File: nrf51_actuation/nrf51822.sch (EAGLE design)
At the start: 22 parts, among them T1 MMUN2238

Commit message: Sensor board should be 100% done... Waiting for boards from slow china :0)
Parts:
- removed CR2450: 3.3V, NordicSemi:CR2450
- removed PIR: EKMB1303112, NordicSemi:EKMB1303112
- removed SI7021: SI7021SMD, NordicSemi:SI7021SMD
- removed SW1: (no value), microbuilder:SWITCH_PUSHBUTTONSOFTTOUCHSMD_SJ
- removed TMP36: TMP36_SOT23_5, NordicSemi:TMP36_SOT23_5
- removed TSL2561: LIGHT_TSL2561, microbuilder:LIGHT_TSL2561
- removed U$6, U$7: MOUNTINGHOLE2.5, microbuilder:MOUNTINGHOLE2.5
- added ACS712_20A: ACS712, SparkFun-AnalogIC:ACS712
- added ADP121: (no value), microbuilder:ADP121
- added C4, C5: 10uF, rcl:C-EUC0805
- added FTR-K3AB: FTR-K3AB, NordicSemi:FTR-K3AB
- added J1, J2, J3, J4: (no value), microbuilder:TERMBLOCK_1X2
- added R1, R2: (no value), microbuilder:RESISTOR0805
- C1: value 100nF -> 1nF
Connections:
- removed net GIOP3: SW1.P$2, U$4.P0.11
- new net 5.0V: ACS712_20A.VCC, ADP121.EN, ADP121.IN, C2.1, C5.1, FTR-K3ABG$2.1, J3.1
- new net N$11: ACS712_20A.FILT, C1.1
- new net N$15: ACS712_20A.VOUT, R1.1
- new net ROUT1: ACS712_20A.IP+@1, ACS712_20A.IP+@2, FTR-K3ABG$1.4, J2.1, J4.1
- new net ROUT2: ACS712_20A.IP-@3, ACS712_20A.IP-@4, FTR-K3ABG$1.3, J2.2, J4.2
- new net TERMO1: J1.1
- new net TERMO2: J1.2
- net AIN0/XL2: now also R1.2, R2.1
- net AIN2: no longer TMP36.+VS, TMP36.SHTD
- net AIN3: no longer TMP36.VOUT
- net AIN5: no longer PIR.OUT
- net AIN6: no longer PIR.VDD
- net GIOP0: no longer TSL2561.SDA
- net GIOP1: no longer TSL2561.SCL
- net GIOP5: no longer SI7021.SDA
- net GIOP6: no longer SI7021.SCL
- net GIOP7: no longer C2.1, SI7021.VDD
- net GND: now also ACS712_20A.GND, ADP121.GND, C1.2, C4.2, C5.2, J3.2, R2.2; no longer PIR.GND, SI7021.GND, SW1.P$1, TMP36.GND
- net N$7: now also FTR-K3ABG$2.2; no longer C1.1, TSL2561.GND
- net VDD: now also ADP121.OUT, C4.1; no longer C1.2, TSL2561.3.3V
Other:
- note removed: "BATT"
- note removed: "HIGH DRIVE"
- note removed: "HUMIDITY+TEMP"
- note removed: "LIGHT"
- note removed: "NC"
- note removed: "TEMP"
- note removed: "USE INTERNAL PULLUP"
- moved on the sheet: C1, C2, T1

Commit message: Done with routing.. should be more or less done
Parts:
- removed J3: (no value), microbuilder:TERMBLOCK_1X2
- added AD8495: AD8495, NordicSemi:AD8495
- added C12: 100nF, rcl:C-EUC0805
- added C13, C14: 12pF, rcl:C-EUC0805
- added C6: 10nF, rcl:C-EUC0805
- added FB1, FB2: (no value), microbuilder:FERRITE0805
- added IRM-05-5: IRM05-5V, NordicSemi:IRM05-5V
- added U$1, U$13, U$14, U$7: MOUNTINGHOLE2.5, microbuilder:MOUNTINGHOLE2.5
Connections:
- removed net ROUT1: ACS712_20A.IP+@1, ACS712_20A.IP+@2, FTR-K3ABG$1.4, J2.1, J4.1
- removed net ROUT2: ACS712_20A.IP-@3, ACS712_20A.IP-@4, FTR-K3ABG$1.3, J2.2, J4.2
- removed net TERMO1: J1.1
- removed net TERMO2: J1.2
- new net AC/L: ACS712_20A.IP+@1, ACS712_20A.IP+@2, IRM-05-5.AC/L, J4.1
- new net AC/LOUT: ACS712_20A.IP-@3, ACS712_20A.IP-@4, J2.2
- new net AC/N: FTR-K3ABG$1.3, IRM-05-5.AC/N, J4.2
- new net AC/NOUT: FTR-K3ABG$1.4, J2.1
- new net GIOP10: U$4.P0.17
- new net GIOP3: U$4.P0.11
- new net N$16: AD8495.-IN, C6.2, FB2.P$2
- new net N$17: FB2.P$1, J1.2
- new net N$8: FB1.P$1, J1.1
- new net N$9: AD8495.+IN, C6.1, FB1.P$2
- net 5.0V: now also AD8495.+VS, C12.2, IRM-05-5.+V; no longer J3.1
- net AIN4: now also AD8495.OUT, AD8495.SENSE
- net GND: now also AD8495.GND, AD8495.REF, C12.1, C13.1, C14.1, IRM-05-5.-V; no longer J3.2
- net N$1: now also C14.2, CRST1.H2, U$4.XC2; no longer CRST1.H1, U$4.XC1
- net N$2: now also C13.2, CRST1.H1, U$4.XC1; no longer CRST1.H2, U$4.XC2
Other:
- note added: "THERMO"
- moved on the sheet: ANT, BALUN, C10, C11, C3, C7, C8, C9, CRST1, J1, J2, J4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

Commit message: CLEANED AND ADDED COMMENTS / TAGS ACTUATION MADE 45% SMALLER
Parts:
- removed U$13, U$14: MOUNTINGHOLE2.5, microbuilder:MOUNTINGHOLE2.5
- R1: value (none) -> 2k
- R2: value (none) -> 8k
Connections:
- net AC/L: now also FTR-K3ABG$1.4; no longer ACS712_20A.IP+@1, ACS712_20A.IP+@2
- net AC/LOUT: now also FTR-K3ABG$1.3, J2.1; no longer ACS712_20A.IP-@3, ACS712_20A.IP-@4, J2.2
- net AC/N: now also ACS712_20A.IP+@1, ACS712_20A.IP+@2; no longer FTR-K3ABG$1.3
- net AC/NOUT: now also ACS712_20A.IP-@3, ACS712_20A.IP-@4, J2.2; no longer FTR-K3ABG$1.4, J2.1
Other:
- note added: "AC IN"
- note added: "AC OUT"
- note added: "AC/DC"
- note added: "DC/DC"
- note added: "HALL EFFECT"
- note added: "MOUNT HOLES"
- note added: "PROG HEADER"
- note added: "RELAY"
- note added: "THERMOCOUPLE COLD JUNCTION"
- note removed: "THERMO"
- moved on the sheet: AD8495, C12, C6, FB1, FB2, J1, J2

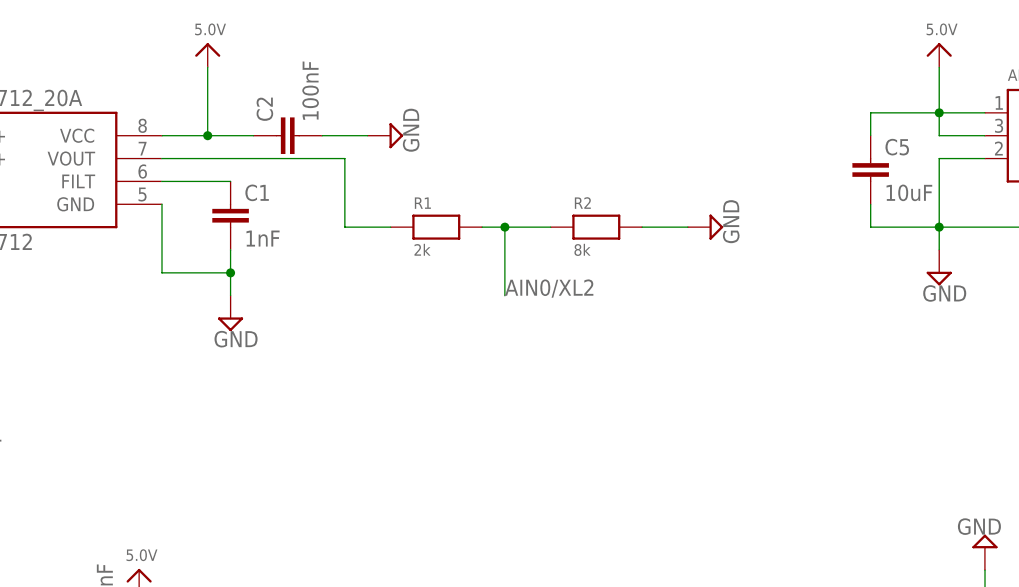
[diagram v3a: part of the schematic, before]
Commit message: Added optional low pass filter circut and cleaned up some more
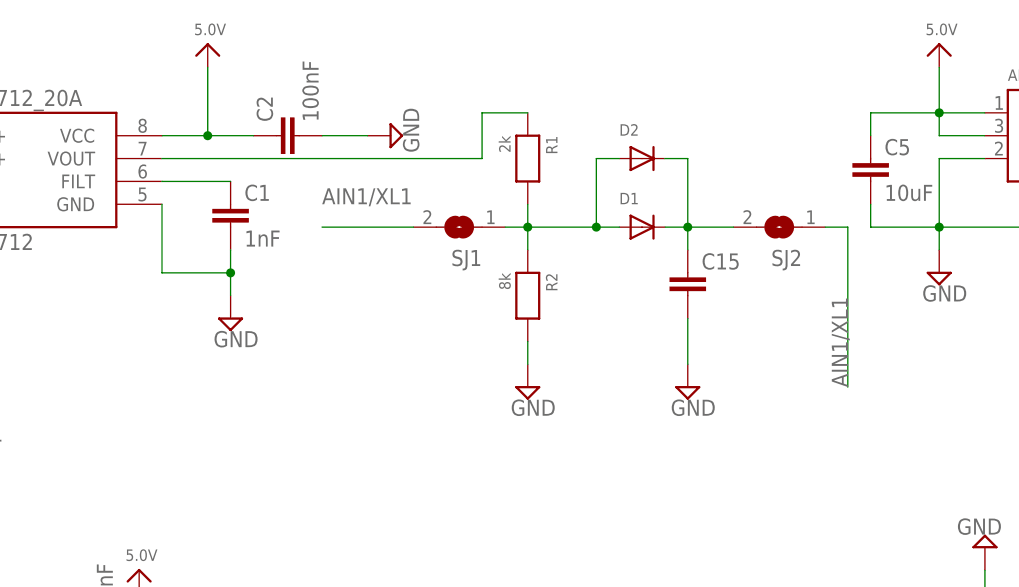
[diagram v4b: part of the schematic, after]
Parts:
- added C15: (no value), SparkFun-Capacitors:CAPPTH3
- added D1: (no value), adafruit:DIODESOD-123
- added D2: (no value), microbuilder:DIODEDO-1N4148
- added SJ1, SJ2: SOLDERJUMPERREFLOW_NOPASTE, microbuilder:SOLDERJUMPERREFLOW_NOPASTE
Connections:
- new net N$15: D1.A, D2.A, R1.2, R2.1, SJ1.1
- new net N$19: C15.1, D1.C, D2.C, SJ2.2
- net AIN0/XL2: no longer R1.2, R2.1
- net AIN1/XL1: now also SJ1.2, SJ2.1
- net GND: now also C15.2
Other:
- moved on the sheet: R1, R2
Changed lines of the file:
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@@
 <part name="U$1" library="microbuilder" deviceset="MOUNTINGHOLE" device="2.5"/>
 <part name="U$7" library="microbuilder" deviceset="MOUNTINGHOLE" device="2.5"/>
+<part name="SJ2" library="microbuilder" deviceset="SOLDERJUMPER" device="REFLOW_NOPASTE"/>
+<part name="D1" library="adafruit" deviceset="DIODE" device="SOD-123"/>
+<part name="C15" library="SparkFun-Capacitors" deviceset="CAP" device="PTH3"/>
+<part name="D2" library="microbuilder" deviceset="DIODE" device="DO-1N4148"/>
+<part name="SUPPLY14" library="supply2" deviceset="GND" device=""/>
+<part name="SJ1" library="microbuilder" deviceset="SOLDERJUMPER" device="REFLOW_NOPASTE"/>
 </parts>
 <sheets>
@@
 <instance part="FRAME1" gate="G$1" x="-88.9" y="-20.32"/>
 <instance part="ACS712_20A" gate="G$1" x="-43.18" y="139.7"/>
-<instance part="R1" gate="G$1" x="0" y="134.62"/>
-<instance part="R2" gate="G$1" x="17.78" y="134.62"/>
+<instance part="R1" gate="G$1" x="10.16" y="142.24" rot="R270"/>
+<instance part="R2" gate="G$1" x="10.16" y="127" rot="R270"/>
 <instance part="SUPPLY13" gate="GND" x="-22.86" y="124.46"/>
 <instance part="C1" gate="G$1" x="-22.86" y="137.16"/>
@@
 <instance part="SUPPLY15" gate="GND" x="-5.08" y="144.78" rot="R90"/>
 <instance part="U$8" gate="G$1" x="-25.4" y="154.94"/>
-<instance part="SUPPLY6" gate="GND" x="30.48" y="134.62" rot="R90"/>
+<instance part="SUPPLY6" gate="GND" x="10.16" y="116.84"/>
 <instance part="J4" gate="G$1" x="121.92" y="137.16" rot="MR0"/>
 <instance part="FTR-K3AB" gate="G$1" x="-48.26" y="15.24" rot="R270"/>
@@
 <instance part="U$1" gate="G$1" x="160.02" y="10.16"/>
 <instance part="U$7" gate="G$1" x="177.8" y="10.16"/>
+<instance part="SJ2" gate="1" x="38.1" y="134.62" smashed="yes" rot="R180">
+<attribute name="NAME" x="40.64" y="132.08" size="1.778" layer="95" rot="R180"/>
+</instance>
+<instance part="D1" gate="G$1" x="22.86" y="134.62"/>
+<instance part="C15" gate="G$1" x="27.94" y="127"/>
+<instance part="D2" gate="G$1" x="22.86" y="142.24"/>
+<instance part="SUPPLY14" gate="GND" x="27.94" y="116.84"/>
+<instance part="SJ1" gate="1" x="2.54" y="134.62" smashed="yes" rot="R180">
+<attribute name="NAME" x="5.08" y="132.08" size="1.778" layer="95" rot="R180"/>
+</instance>
 </instances>
 <busses>
@@
 <pinref part="R2" gate="G$1" pin="2"/>
 <pinref part="SUPPLY6" gate="GND" pin="GND"/>
-<wire x1="22.86" y1="134.62" x2="27.94" y2="134.62" width="0.1524" layer="91"/>
+<wire x1="10.16" y1="121.92" x2="10.16" y2="119.38" width="0.1524" layer="91"/>
 </segment>
 <segment>
@@
 <junction x="86.36" y="119.38"/>
 </segment>
+<segment>
+<pinref part="C15" gate="G$1" pin="2"/>
+<pinref part="SUPPLY14" gate="GND" pin="GND"/>
+<wire x1="27.94" y1="124.46" x2="27.94" y2="119.38" width="0.1524" layer="91"/>
+</segment>
 </net>
 <net name="VDD" class="0">
@@
 <net name="AIN0/XL2" class="0">
 <segment>
-<pinref part="R1" gate="G$1" pin="2"/>
-<pinref part="R2" gate="G$1" pin="1"/>
-<wire x1="5.08" y1="134.62" x2="7.62" y2="134.62" width="0.1524" layer="91"/>
-<wire x1="7.62" y1="134.62" x2="12.7" y2="134.62" width="0.1524" layer="91"/>
-<wire x1="7.62" y1="134.62" x2="7.62" y2="127" width="0.1524" layer="91"/>
-<junction x="7.62" y="134.62"/>
-<label x="7.62" y="127" size="1.778" layer="95"/>
-</segment>
-<segment>
 <pinref part="U$4" gate="G$1" pin="P0.26"/>
 <wire x1="58.42" y1="81.28" x2="58.42" y2="83.82" width="0.1524" layer="91"/>
@@
 </segment>
 </net>
-<net name="N$15" class="0">
-<segment>
-<pinref part="ACS712_20A" gate="G$1" pin="VOUT"/>
-<wire x1="-30.48" y1="142.24" x2="-10.16" y2="142.24" width="0.1524" layer="91"/>
-<wire x1="-10.16" y1="142.24" x2="-10.16" y2="134.62" width="0.1524" layer="91"/>
-<pinref part="R1" gate="G$1" pin="1"/>
-<wire x1="-10.16" y1="134.62" x2="-5.08" y2="134.62" width="0.1524" layer="91"/>
-</segment>
-</net>
 <net name="N$7" class="0">
 <segment>
@@
 <wire x1="55.88" y1="81.28" x2="55.88" y2="83.82" width="0.1524" layer="91"/>
 <label x="55.88" y="78.74" size="1.778" layer="95" rot="R90"/>
+</segment>
+<segment>
+<pinref part="SJ2" gate="1" pin="1"/>
+<wire x1="43.18" y1="134.62" x2="45.72" y2="134.62" width="0.1" layer="91"/>
+<wire x1="45.72" y1="134.62" x2="45.72" y2="116.84" width="0.1" layer="91"/>
+<label x="45.72" y="116.84" size="1.778" layer="95" rot="R90"/>
+</segment>
+<segment>
+<pinref part="SJ1" gate="1" pin="2"/>
+<wire x1="-2.54" y1="134.62" x2="-12.7" y2="134.62" width="0.1" layer="91"/>
+<label x="-12.7" y="137.16" size="1.778" layer="95"/>
 </segment>
 </net>
@@
 </segment>
 </net>
+<net name="N$18" class="0">
+<segment>
+<pinref part="ACS712_20A" gate="G$1" pin="VOUT"/>
+<wire x1="-30.48" y1="142.24" x2="5.08" y2="142.24" width="0.1524" layer="91"/>
+<wire x1="5.08" y1="142.24" x2="5.08" y2="147.32" width="0.1524" layer="91"/>
+<pinref part="R1" gate="G$1" pin="1"/>
+<wire x1="5.08" y1="147.32" x2="10.16" y2="147.32" width="0.1524" layer="91"/>
+</segment>
+</net>
+<net name="N$19" class="0">
+<segment>
+<pinref part="D2" gate="G$1" pin="C"/>
+<wire x1="25.4" y1="142.24" x2="27.94" y2="142.24" width="0.1524" layer="91"/>
+<pinref part="D1" gate="G$1" pin="C"/>
+<pinref part="SJ2" gate="1" pin="2"/>
+<wire x1="25.4" y1="134.62" x2="27.94" y2="134.62" width="0.1524" layer="91"/>
+<pinref part="C15" gate="G$1" pin="1"/>
+<wire x1="27.94" y1="134.62" x2="33.02" y2="134.62" width="0.1524" layer="91"/>
+<wire x1="27.94" y1="132.08" x2="27.94" y2="134.62" width="0.1524" layer="91"/>
+<junction x="27.94" y="134.62"/>
+<wire x1="27.94" y1="142.24" x2="27.94" y2="134.62" width="0.1524" layer="91"/>
+</segment>
+</net>
+<net name="N$15" class="0">
+<segment>
+<pinref part="R1" gate="G$1" pin="2"/>
+<pinref part="R2" gate="G$1" pin="1"/>
+<wire x1="10.16" y1="137.16" x2="10.16" y2="134.62" width="0.1" layer="91"/>
+<pinref part="SJ1" gate="1" pin="1"/>
+<pinref part="D1" gate="G$1" pin="A"/>
+<wire x1="10.16" y1="134.62" x2="10.16" y2="132.08" width="0.1" layer="91"/>
+<wire x1="7.62" y1="134.62" x2="10.16" y2="134.62" width="0.1" layer="91"/>
+<junction x="10.16" y="134.62"/>
+<wire x1="10.16" y1="134.62" x2="17.78" y2="134.62" width="0.1" layer="91"/>
+<pinref part="D2" gate="G$1" pin="A"/>
+<wire x1="17.78" y1="134.62" x2="20.32" y2="134.62" width="0.1" layer="91"/>
+<wire x1="20.32" y1="142.24" x2="17.78" y2="142.24" width="0.1" layer="91"/>
+<wire x1="17.78" y1="142.24" x2="17.78" y2="134.62" width="0.1" layer="91"/>
+<junction x="17.78" y="134.62"/>
+</segment>
+</net>

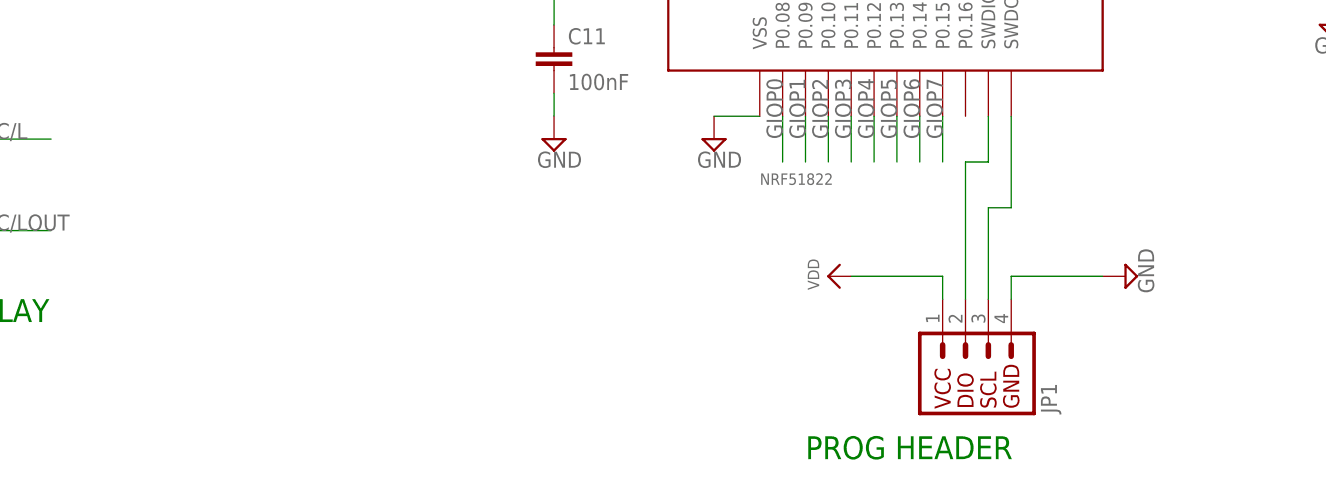
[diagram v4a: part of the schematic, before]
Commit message: Added a TMP36 sensor to ensure a power cutoff if the temperature rises above a threshold (in case of fire or shortcut)
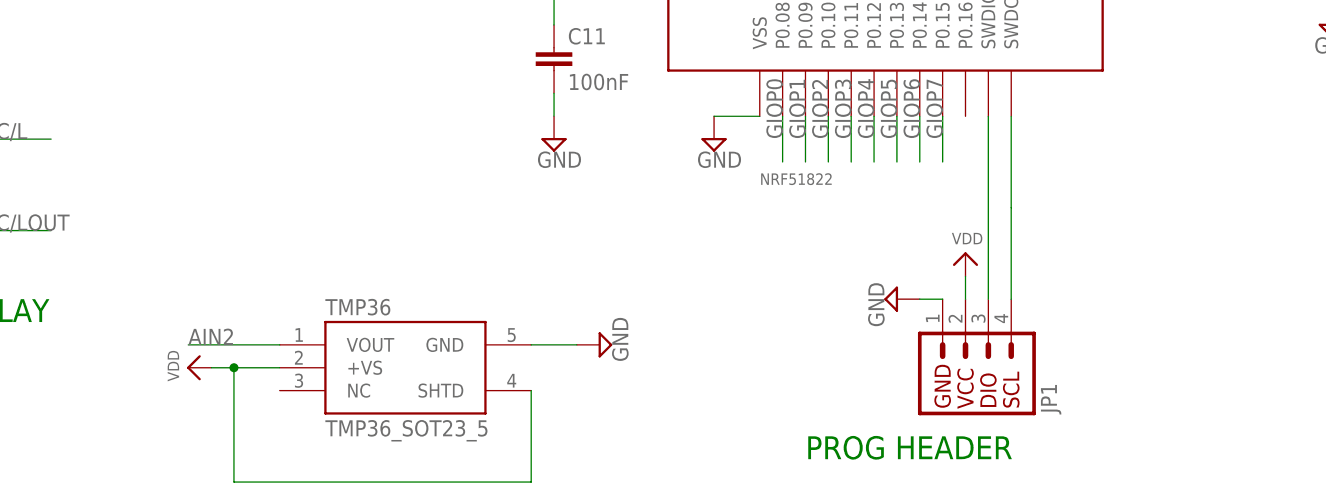
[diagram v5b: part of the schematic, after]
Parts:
- added TMP36: TMP36_SOT23_5, NordicSemi:TMP36_SOT23_5
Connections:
- net AIN2: now also TMP36.VOUT
- net GND: now also JP1.1, TMP36.GND; no longer JP1.4
- net N$12: now also JP1.3; no longer JP1.2
- net N$14: now also JP1.4; no longer JP1.3
- net VDD: now also JP1.2, TMP36.+VS, TMP36.SHTD; no longer JP1.1
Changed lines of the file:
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@@
 <part name="SUPPLY14" library="supply2" deviceset="GND" device=""/>
 <part name="SJ1" library="microbuilder" deviceset="SOLDERJUMPER" device="REFLOW_NOPASTE"/>
+<part name="TMP36" library="NordicSemi" deviceset="TMP36_SOT23_5" device=""/>
+<part name="SUPPLY20" library="supply2" deviceset="GND" device=""/>
+<part name="U$14" library="microbuilder" deviceset="VDD" device=""/>
 </parts>
 <sheets>
@@
 <instance part="BG" gate="G$1" x="119.38" y="99.06"/>
 <instance part="U$5" gate="G$1" x="27.94" y="43.18"/>
-<instance part="SUPPLY19" gate="GND" x="91.44" y="5.08" rot="R90"/>
-<instance part="U$3" gate="G$1" x="58.42" y="5.08" rot="R90"/>
+<instance part="SUPPLY19" gate="GND" x="66.04" y="2.54" rot="R270"/>
+<instance part="U$3" gate="G$1" x="73.66" y="7.62"/>
 <instance part="JP1" gate="G$1" x="68.58" y="-7.62" rot="MR90"/>
 <instance part="SUPPLY21" gate="GND" x="86.36" y="121.92" rot="R180"/>
@@
 <attribute name="NAME" x="5.08" y="132.08" size="1.778" layer="95" rot="R180"/>
 </instance>
+<instance part="TMP36" gate="G$1" x="10.16" y="-5.08"/>
+<instance part="SUPPLY20" gate="GND" x="33.02" y="-2.54" rot="R90"/>
+<instance part="U$14" gate="G$1" x="-12.7" y="-5.08" rot="R90"/>
 </instances>
 <busses>
@@
 </segment>
 <segment>
-<pinref part="SUPPLY19" gate="GND" pin="GND"/>
-<pinref part="JP1" gate="G$1" pin="4"/>
-<wire x1="88.9" y1="5.08" x2="78.74" y2="5.08" width="0.1524" layer="91"/>
-<wire x1="78.74" y1="5.08" x2="78.74" y2="2.54" width="0.1524" layer="91"/>
-</segment>
-<segment>
 <pinref part="C14" gate="G$1" pin="1"/>
 <pinref part="SUPPLY21" gate="GND" pin="GND"/>
@@
 <pinref part="SUPPLY14" gate="GND" pin="GND"/>
 <wire x1="27.94" y1="124.46" x2="27.94" y2="119.38" width="0.1524" layer="91"/>
+</segment>
+<segment>
+<pinref part="TMP36" gate="G$1" pin="GND"/>
+<pinref part="SUPPLY20" gate="GND" pin="GND"/>
+<wire x1="25.4" y1="-2.54" x2="30.48" y2="-2.54" width="0.1" layer="91"/>
+</segment>
+<segment>
+<pinref part="JP1" gate="G$1" pin="1"/>
+<pinref part="SUPPLY19" gate="GND" pin="GND"/>
+<wire x1="71.12" y1="2.54" x2="68.58" y2="2.54" width="0.1" layer="91"/>
 </segment>
 </net>
@@
 </segment>
 <segment>
+<pinref part="TMP36" gate="G$1" pin="+VS"/>
+<pinref part="U$14" gate="G$1" pin="VDD"/>
+<wire x1="-2.54" y1="-5.08" x2="-7.62" y2="-5.08" width="0.1" layer="91"/>
+<pinref part="TMP36" gate="G$1" pin="SHTD"/>
+<wire x1="-7.62" y1="-5.08" x2="-10.16" y2="-5.08" width="0.1" layer="91"/>
+<wire x1="25.4" y1="-7.62" x2="25.4" y2="-17.78" width="0.1" layer="91"/>
+<wire x1="25.4" y1="-17.78" x2="-7.62" y2="-17.78" width="0.1" layer="91"/>
+<wire x1="-7.62" y1="-17.78" x2="-7.62" y2="-5.08" width="0.1" layer="91"/>
+<junction x="-7.62" y="-5.08"/>
+</segment>
+<segment>
 <pinref part="U$3" gate="G$1" pin="VDD"/>
-<pinref part="JP1" gate="G$1" pin="1"/>
-<wire x1="60.96" y1="5.08" x2="71.12" y2="5.08" width="0.1524" layer="91"/>
-<wire x1="71.12" y1="5.08" x2="71.12" y2="2.54" width="0.1524" layer="91"/>
+<pinref part="JP1" gate="G$1" pin="2"/>
+<wire x1="73.66" y1="5.08" x2="73.66" y2="2.54" width="0.1" layer="91"/>
 </segment>
 </net>
@@
 <label x="30.48" y="55.88" size="1.778" layer="95"/>
 </segment>
+<segment>
+<pinref part="TMP36" gate="G$1" pin="VOUT"/>
+<wire x1="-2.54" y1="-2.54" x2="-12.7" y2="-2.54" width="0.1" layer="91"/>
+<label x="-12.7" y="-2.54" size="1.778" layer="95"/>
+</segment>
 </net>
 <net name="AIN3" class="0">
@@
 <pinref part="U$4" gate="G$1" pin="SWDIO/NRESET"/>
 <wire x1="76.2" y1="22.86" x2="76.2" y2="17.78" width="0.1524" layer="91"/>
-<pinref part="JP1" gate="G$1" pin="2"/>
-<wire x1="76.2" y1="17.78" x2="73.66" y2="17.78" width="0.1524" layer="91"/>
-<wire x1="73.66" y1="17.78" x2="73.66" y2="2.54" width="0.1524" layer="91"/>
+<pinref part="JP1" gate="G$1" pin="3"/>
+<wire x1="76.2" y1="17.78" x2="76.2" y2="2.54" width="0.1" layer="91"/>
 </segment>
 </net>
@@
 <pinref part="U$4" gate="G$1" pin="SWDCLK"/>
 <wire x1="78.74" y1="22.86" x2="78.74" y2="12.7" width="0.1524" layer="91"/>
-<pinref part="JP1" gate="G$1" pin="3"/>
-<wire x1="78.74" y1="12.7" x2="76.2" y2="12.7" width="0.1524" layer="91"/>
-<wire x1="76.2" y1="12.7" x2="76.2" y2="2.54" width="0.1524" layer="91"/>
-</segment>
-</net>
+<pinref part="JP1" gate="G$1" pin="4"/>
+<wire x1="78.74" y1="12.7" x2="78.74" y2="2.54" width="0.1" layer="91"/>
+</segment>
+</net>

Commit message: Sent to smart-prototype Actuation 1.2 Compact 1.1
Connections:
- net AC/L: now also FTR-K3ABG$1.3; no longer FTR-K3ABG$1.4
- net AC/LOUT: now also FTR-K3ABG$1.4; no longer FTR-K3ABG$1.3
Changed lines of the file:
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@@
 </segment>
 <segment>
-<pinref part="FTR-K3AB" gate="G$1" pin="4"/>
-<wire x1="-43.18" y1="20.32" x2="-27.94" y2="20.32" width="0.1524" layer="91"/>
-<label x="-35.56" y="20.32" size="1.778" layer="95"/>
+<pinref part="FTR-K3AB" gate="G$1" pin="3"/>
+<wire x1="-43.18" y1="10.16" x2="-27.94" y2="10.16" width="0.1524" layer="91"/>
+<label x="-35.56" y="10.16" size="1.778" layer="95"/>
 </segment>
 </net>
@@
 </segment>
 <segment>
-<pinref part="FTR-K3AB" gate="G$1" pin="3"/>
-<wire x1="-43.18" y1="10.16" x2="-27.94" y2="10.16" width="0.1524" layer="91"/>
-<label x="-35.56" y="10.16" size="1.778" layer="95"/>
+<pinref part="FTR-K3AB" gate="G$1" pin="4"/>
+<wire x1="-43.18" y1="20.32" x2="-27.94" y2="20.32" width="0.1524" layer="91"/>
+<label x="-35.56" y="20.32" size="1.778" layer="95"/>
 </segment>
 </net>
